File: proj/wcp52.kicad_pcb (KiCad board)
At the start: 4 copper layers, 100 x 100 mm, 321 parts, among them J1 MicroUSB-B, J2 IN1, J3 IN2, J4 OUT, J5 CONN-PJ-037A, J6 JLINK, J7 AUX, Q1 MMBT3906, Q10 MMBT3904, Q11 BFR540, Q12 BFR540, Q13 MMBT3904, Q14 MMBT3904, Q15 MMBT3904, Q16 MMBT3904, Q17 PZT2907A, Q18 PZT2907A, Q19 MMBT3904, Q2 IRLML6402, Q3 AOD417, Q4 MMBT3906, Q5 2N7002, Q6 2N7002, Q7 MMBT3906, Q8 2N7002, Q9 2N7002, U1 TL431AIDBZ, U10 MASWSS0162, U11 AD8310ARMZ, U12 ATSAM4S16CA-AU, U13 FT230XS_DNP, U14 L78M05CDT, U15 MC79M05CDT, U16 AZ1117CH-1.8TRG1, U17 MCP1700T-vv02E/TT, U2 LM393M, U3 LMH6714MF, U4 AD9958BCPZ, U5 LMH6714MF, U6 AD8000YRDZ, U7 THS3001IDGN, U8 MAADSS0008, U9 MASWSS0162, X1 25 MHz, X2 12MHz

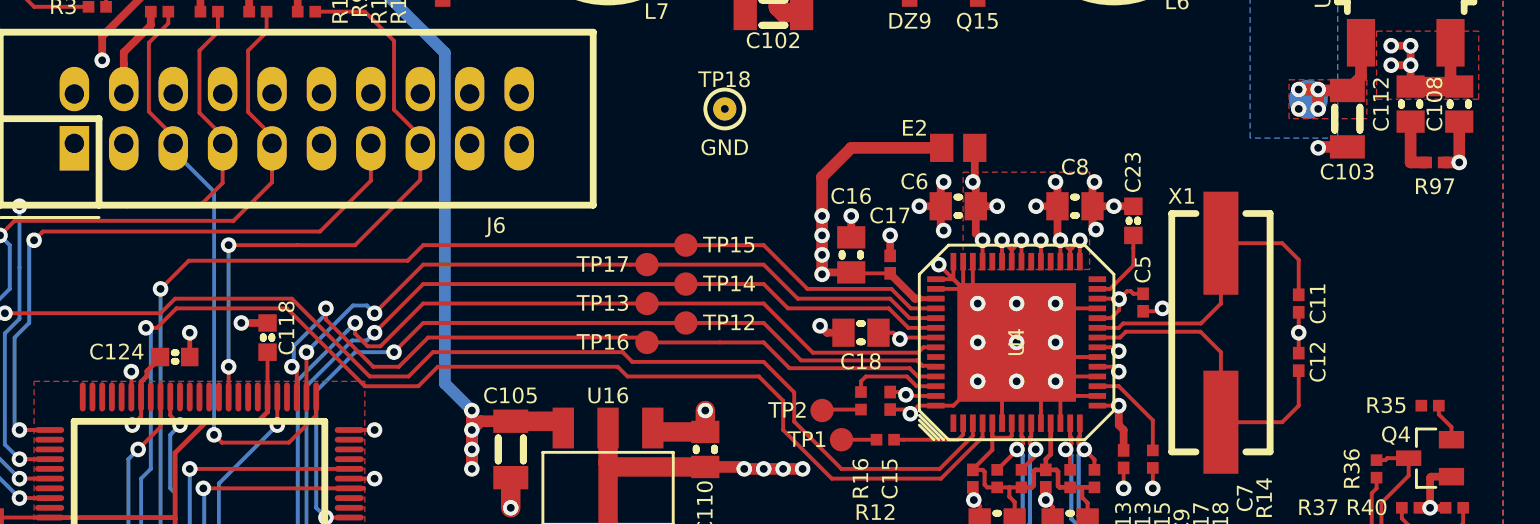
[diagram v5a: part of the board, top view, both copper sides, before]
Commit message: Connect attenuator control
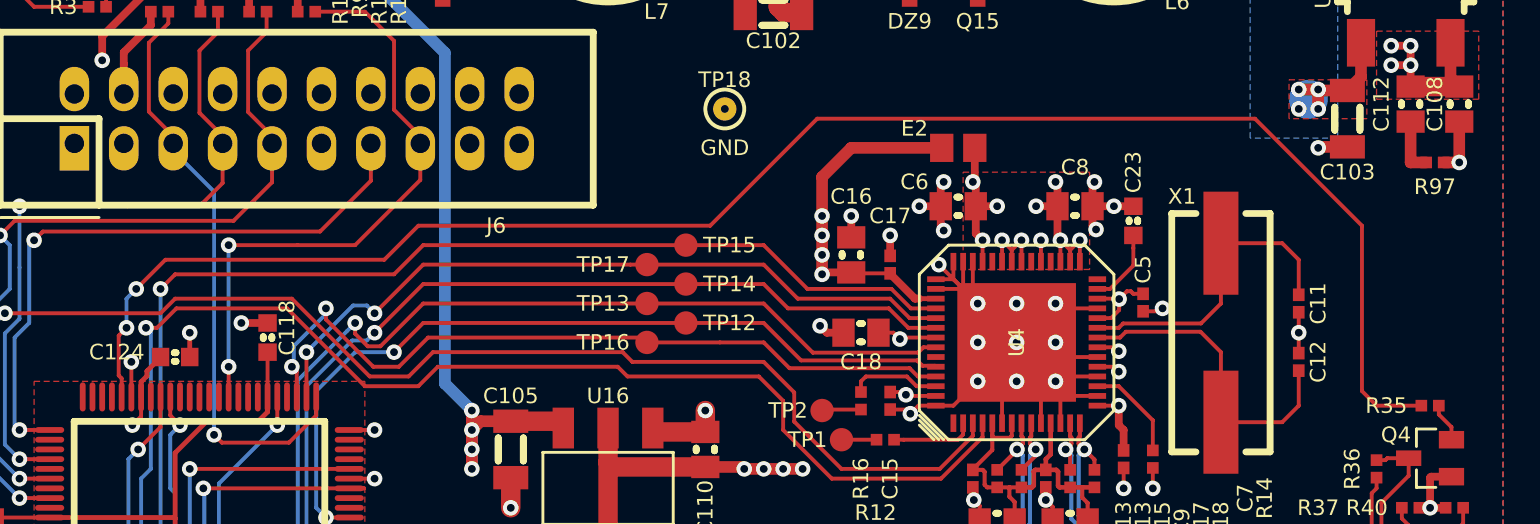
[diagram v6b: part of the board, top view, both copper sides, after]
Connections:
- R35 pad 1: /OutputAmp/ATTEN -> /MPU/ATTEN
- U12 pad 71: Net-(U12-Pad71) -> /MPU/ATTEN
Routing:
- net /MPU/ATTEN: track 0.00 -> 86.7 mm, vias 0 -> 2
- net GND: track 622.6 -> 623.1 mm

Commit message: Add power LED
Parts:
- added DS2: PWR, smd-semi:LED-0603, F.Cu at (157.0, 51.0)
- added R108: 3k3, IPC7351-Nominal:RESC1005X40, F.Cu at (159.0, 51.0)
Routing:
- net GND: track 623.1 -> 628.8 mm
- net Net-(DS2-Pad2): track 0.00 -> 2.17 mm
- net /DCDC/IN: track 105.7 -> 107.8 mm

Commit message: Some work removing unnecessary bits
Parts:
- removed C90, C91: 47p, IPC7351-Nominal:CAPC1005X55
- removed R16: 100, IPC7351-Nominal:RESC1005X40
- removed R89: 2R2, IPC7351-Nominal:RESC1005X40
- C129: moved to F.Cu
- R12: value 100 -> 0R; footprint IPC7351-Nominal:RESC1005X40 -> IPC7351-Nominal:RESC1608X50
- moved C129 62.0 mm to (125.0, 135.1), turned to 0 degrees
- moved R12 17.7 mm to (150.8, 60.0), turned to 270 degrees
- moved C23 1.03 mm to (149.0, 60.0)
- moved C8 1.00 mm to (146.0, 59.5)
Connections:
- C23 pad 2: GND -> Net-(C23-Pad2)
- C92 pad 2: Net-(C92-Pad2) -> GND
- R12 pad 1: Net-(R12-Pad1) -> Net-(C23-Pad2)
- R12 pad 2: Net-(R12-Pad2) -> +1.8A
- TP1 pad 1: Net-(R12-Pad2) -> Net-(TP1-Pad1)
- TP2 pad 1: Net-(R16-Pad1) -> Net-(TP2-Pad1)
- U4 pad 2: Net-(R12-Pad1) -> Net-(TP1-Pad1)
- U4 pad 54: Net-(R16-Pad2) -> Net-(TP2-Pad1)
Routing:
- net GND: track 628.8 -> 625.7 mm, vias 246 -> 243
- net Net-(C92-Pad2): track 1.90 -> 0.00 mm
- net Net-(C23-Pad2): track 0.00 -> 1.75 mm
- net +1.8A: track 58.8 -> 60.3 mm
- net /Comm/OUT_USBD_P: track 10.8 -> 10.3 mm
